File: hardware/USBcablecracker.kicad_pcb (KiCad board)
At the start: 2 copper layers, 100 x 50 mm, 57 parts, among them P1 USB_A, P10 USB_A, P11 USB_B, P12 CONN_01X09, P2 CONN_01X02, P3 USB_B-Micro, P6 CONN_01X09, P7 USB_B-Mini, P8 USB_B-Micro-3.0, P9 USB_TYPEC-S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

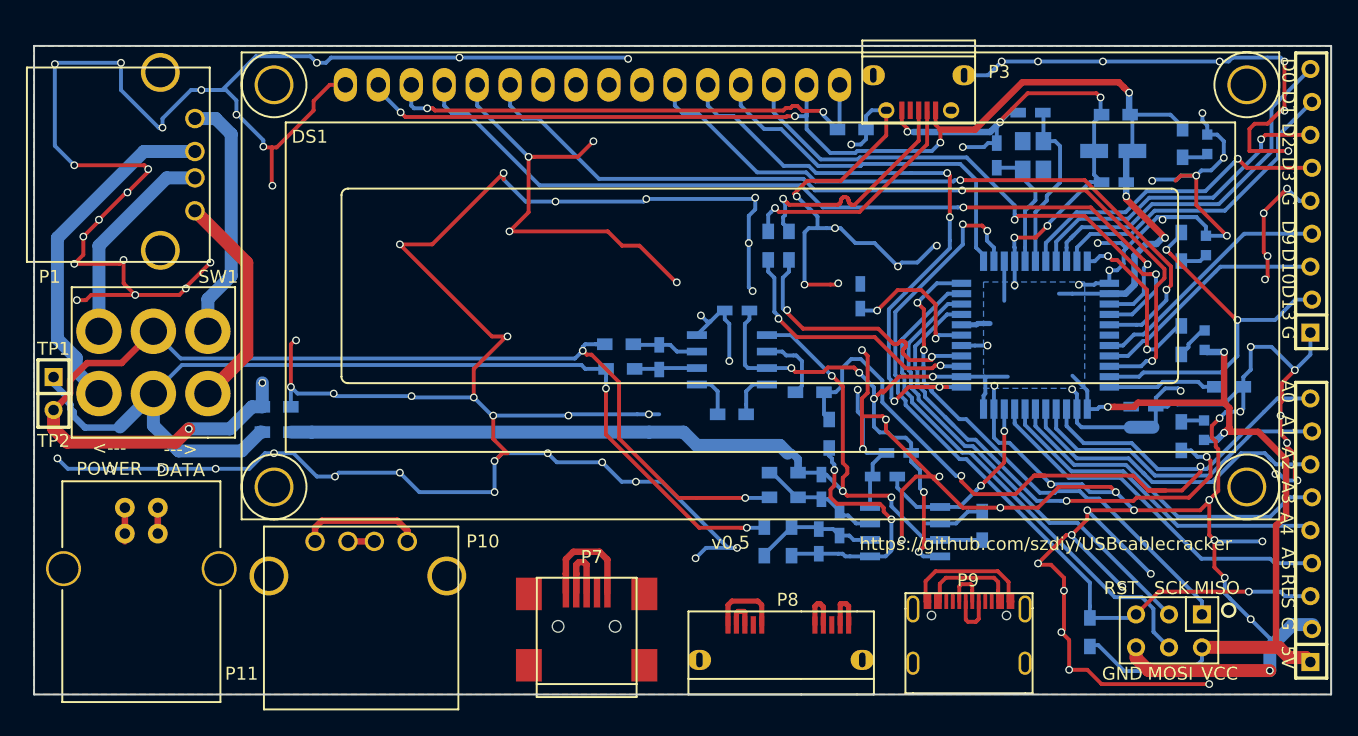
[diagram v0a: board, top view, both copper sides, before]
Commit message: Modify PCB to v2.0, delete switch, add an analog switch and a button instead.
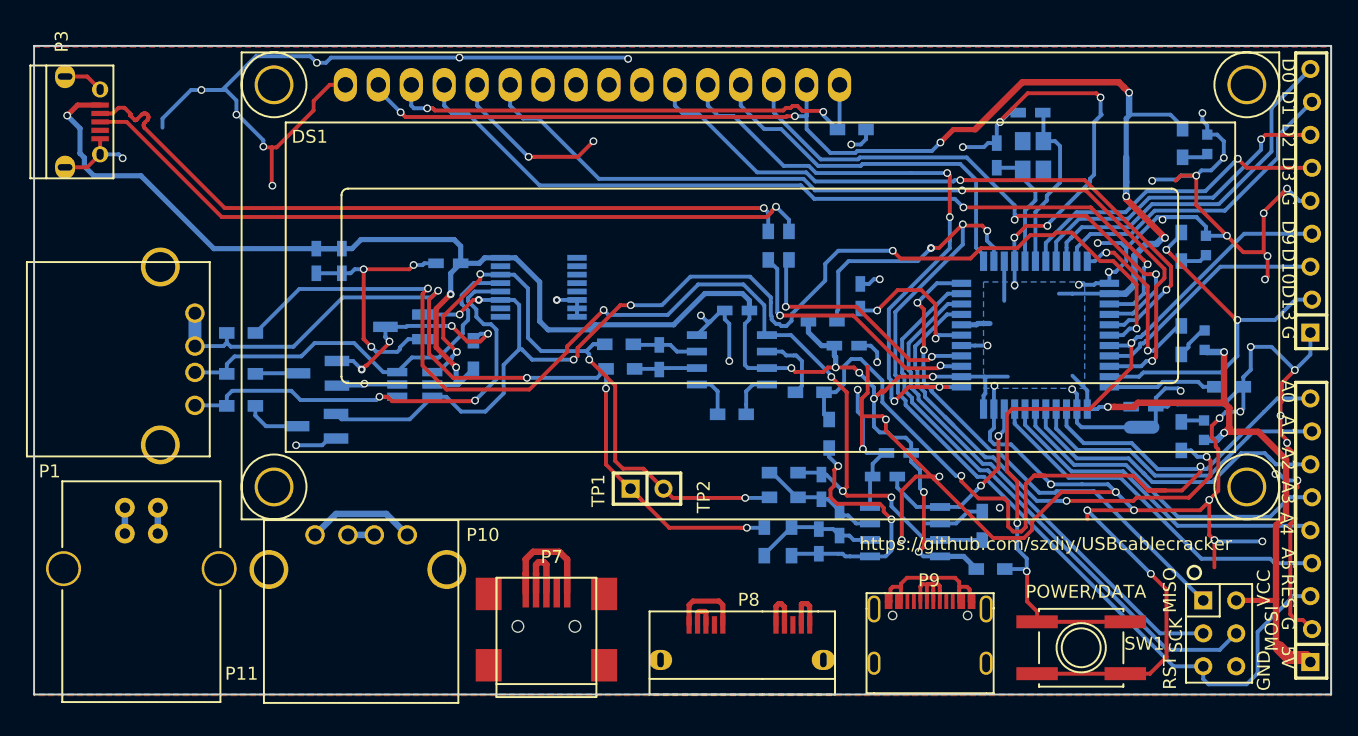
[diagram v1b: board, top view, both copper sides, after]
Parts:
- removed G***: LOGO, USBcablecracker:szdiy_logo
- removed R9: 10K, Resistors_SMD:R_0603_HandSoldering
- added C14: 100nF, Capacitors_SMD:C_0603_HandSoldering, B.Cu at (112.7, 73.1)
- added C15: 100nF, Capacitors_SMD:C_0603_HandSoldering, B.Cu at (81.9, 66.8)
- added Q1: CJ2302, TO_SOT_Packages_SMD:SOT-23_Handsoldering, B.Cu at (71.8, 79.3)
- added Q2: CJ2302, TO_SOT_Packages_SMD:SOT-23_Handsoldering, B.Cu at (71.8, 75.2)
- added Q3: CJ2302, TO_SOT_Packages_SMD:SOT-23_Handsoldering, B.Cu at (78.6, 71.7)
- added R23: 1K, Resistors_SMD:R_0603_HandSoldering, B.Cu at (123.7, 90.3)
- added R24: 33, Resistors_SMD:R_0603_HandSoldering, B.Cu at (66.0, 75.3)
- added R26: 10k, Resistors_SMD:R_0603_HandSoldering, B.Cu at (83.9, 73.8)
- added U4: SN74LVC1G3157, TO_SOT_Packages_SMD:SOT-23-6_Handsoldering, B.Cu at (79.3, 76.1)
- added U5: 4053, Housings_SSOP:TSSOP-16_4.4x5mm_Pitch0.65mm, B.Cu at (88.9, 68.6)
- C8: value 22uF -> 10uF; footprint Capacitors_Tantalum_SMD:Tantalum_Case-A_EIA-3216-18_Wave -> Capacitors_SMD:C_0603_HandSoldering
- DS1: footprint Display:WC1602A -> USBcablecracker:WC1602A
- SW1: value Switch_SPDT_x2 -> SW_SPST; footprint USBcablecracker:DPDT -> Buttons_Switches_SMD:SW_SPST_EVQQ2
- moved SW1 70.1 mm to (130.7, 96.4), turned to 0 degrees
- moved P3 64.7 mm to (53.5, 55.9), turned to 270 degrees
- moved C9 61.8 mm to (71.8, 66.6), turned to 90 degrees
- moved C8 60.1 mm to (73.7, 66.6), turned to 90 degrees
- moved P2 46.3 mm to (97.3, 84.1), turned to 180 degrees
- moved R1 31.6 mm to (110.8, 71.2), turned to 0 degrees
- moved P1 15.0 mm to (62.4, 70.6)
- moved R17 8.12 mm to (66.0, 72.1)
- moved CONN1 3.91 mm to (141.4, 95.3), turned to 180 degrees
- moved P7 3.10 mm to (89.5, 95.6)
- moved P8 3.00 mm to (101.8, 96.2)
- moved P9 3.00 mm to (119.4, 96.2)
- moved R18 2.74 mm to (66.0, 77.8)
- moved P10 0.50 mm to (71.7, 87.7)
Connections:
- C8 pad 1: +5C -> GND
- C8 pad 2: GND -> +5C
- DS1 pad 10: Net-(DS1-Pad10) -> (no net)
- DS1 pad 7: Net-(DS1-Pad7) -> (no net)
- DS1 pad 8: Net-(DS1-Pad8) -> (no net)
- DS1 pad 9: Net-(DS1-Pad9) -> (no net)
- P1 pad 1: Net-(P1-Pad1) -> /TP1
- P1 pad 2: Net-(P1-Pad2) -> /TP1
- P1 pad 3: Net-(P1-Pad3) -> /AX
- P1 pad 4: Net-(P1-Pad4) -> /AY
- P1 pad 5: Net-(P1-Pad5) -> (no net)
- P1 pad 6: Net-(P1-Pad6) -> (no net)
- P10 pad 5: Net-(P10-Pad5) -> (no net)
- P10 pad 6: Net-(P10-Pad6) -> (no net)
- P11 pad 5: Net-(P11-Pad5) -> (no net)
- P11 pad 6: Net-(P11-Pad6) -> (no net)
- P3 pad 4: Net-(P3-Pad4) -> (no net)
- P7 pad 4: Net-(P7-Pad4) -> (no net)
- P7 pad 6: Net-(P7-Pad6) -> (no net)
- P7 pad 7: Net-(P7-Pad7) -> (no net)
- P7 pad 8: Net-(P7-Pad8) -> (no net)
- P7 pad 9: Net-(P7-Pad9) -> (no net)
- P8 pad 11: Net-(P8-Pad11) -> (no net)
- P8 pad 12: Net-(P8-Pad12) -> (no net)
- P8 pad 4: Net-(P8-Pad4) -> (no net)
- P8 pad 8: Net-(P8-Pad8) -> (no net)
- P9 pad 1: Net-(P9-Pad1) -> (no net)
- P9 pad 2: Net-(P9-Pad2) -> (no net)
- P9 pad 3: Net-(P9-Pad3) -> (no net)
- P9 pad 4: Net-(P9-Pad4) -> (no net)
- P9 pad A4: /TEST5 -> /TEST1
- P9 pad A5: Net-(P9-PadA5) -> (no net)
- P9 pad A7: /TEST6 -> /TEST2
- P9 pad A8: Net-(P9-PadA8) -> (no net)
- P9 pad A9: /TEST5 -> /TEST1
- P9 pad B4: /TEST5 -> /TEST1
- P9 pad B5: Net-(P9-PadB5) -> (no net)
- P9 pad B7: /TEST6 -> /TEST2
- P9 pad B8: Net-(P9-PadB8) -> (no net)
- P9 pad B9: /TEST5 -> /TEST1
- R18 pad 1: /TP2 -> /AY
- R18 pad 2: GND -> Net-(Q1-Pad3)
- SW1 pad 1: Net-(P1-Pad4) -> /IO9
- SW1 pad 2: /TP1 -> GND
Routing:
- net GND: track 692.2 -> 395.1 mm, vias 128 -> 65
- net /IO8: track 0.00 -> 95.5 mm, vias 0 -> 6
- net +5C: track 215.3 -> 293.4 mm, vias 15 -> 19
- net /TP2: track 90.8 -> 48.1 mm
- net /DIN-: track 18.7 -> 58.0 mm
- net /DIN+: track 18.7 -> 57.8 mm
- net /IO9: track 19.2 -> 57.7 mm, vias 0 -> 3
- net /AY: track 0.00 -> 37.0 mm, vias 0 -> 2
- net /AX: track 0.00 -> 31.0 mm
- net Net-(P1-Pad2): track 26.7 -> 0.00 mm
- net /RESET: track 61.7 -> 81.4 mm
- net Net-(P1-Pad1): track 19.2 -> 0.00 mm
- net Net-(P1-Pad4): track 17.0 -> 0.00 mm
- net Net-(Q2-Pad1): track 0.00 -> 16.6 mm, vias 0 -> 4
- net Net-(P1-Pad3): track 16.2 -> 0.00 mm
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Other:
- board text added: "POWER/DATA"
- board text added: "V2.0"
- board text removed: "---> DATA"
- board text removed: "<--- POWER"
- board text removed: "V1.0"
- board text removed: "v0.5"
